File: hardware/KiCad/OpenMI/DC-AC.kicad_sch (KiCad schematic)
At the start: 31 parts, among them Q2 IPL60R125P7, Q3 IPL60R125P7, U1 IRS2304S

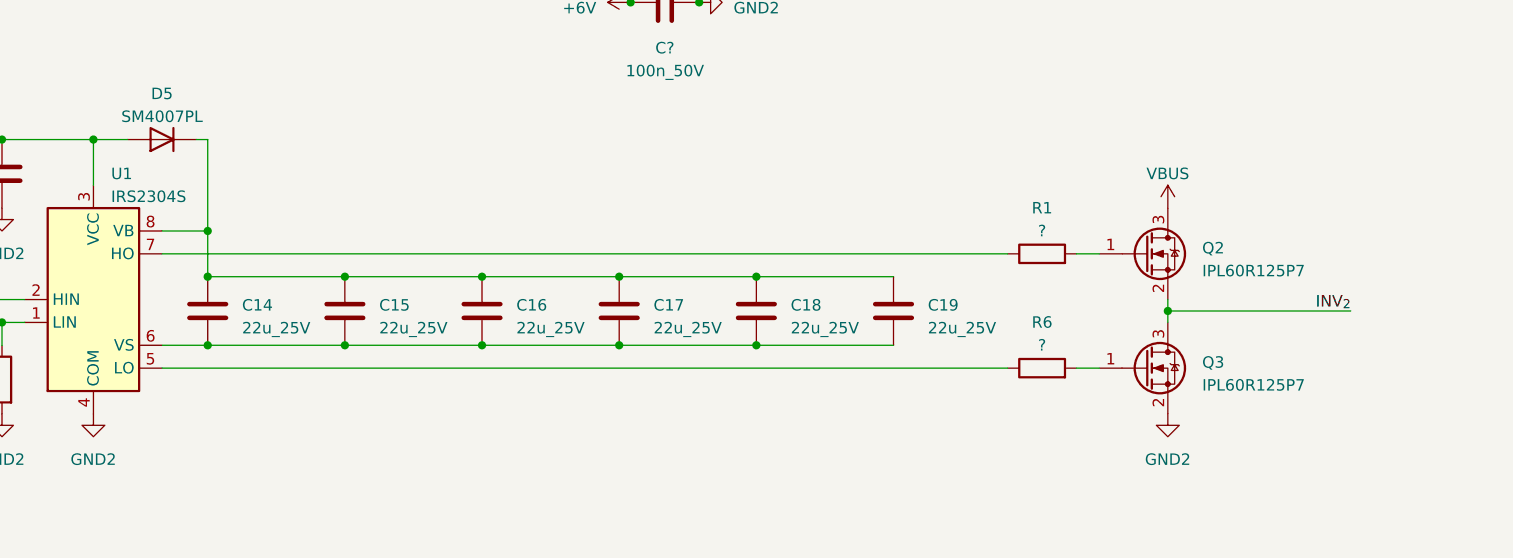
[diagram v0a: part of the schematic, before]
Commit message: fix(hw): connect high-side supply reference with half-bridge output
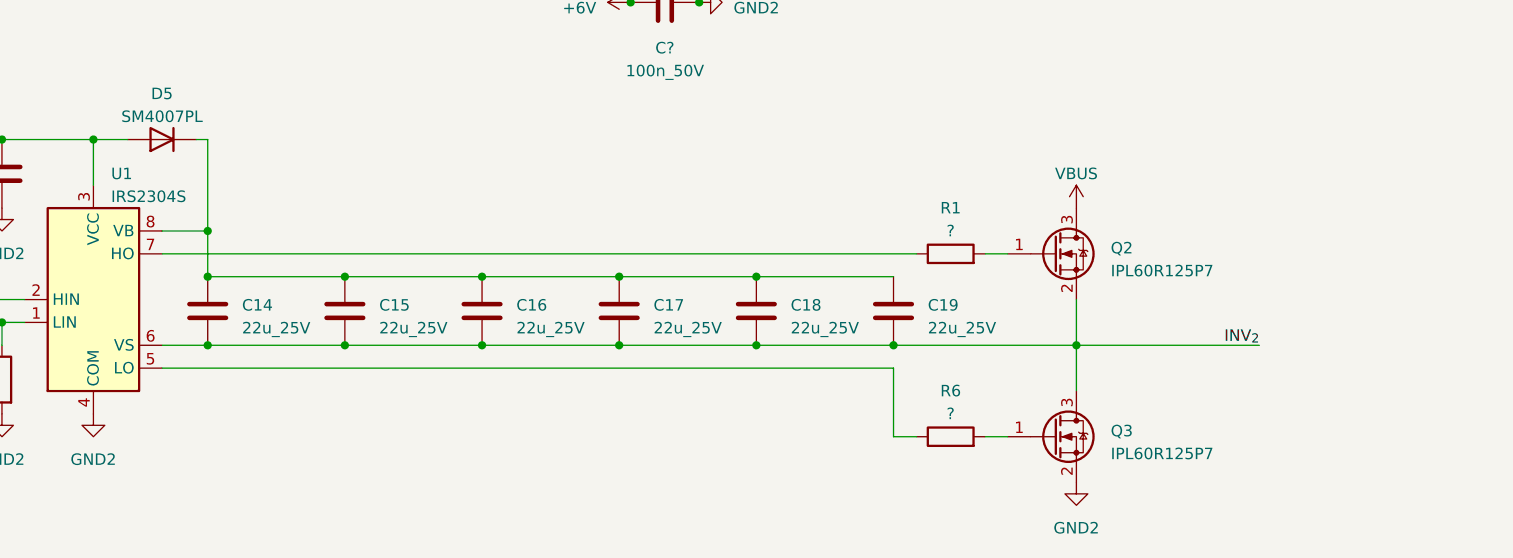
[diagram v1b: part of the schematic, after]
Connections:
- net INV_{2}: now also C14.2, C15.2, C16.2, C17.2, C18.2, C19.2, U1.6 (VS)
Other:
- moved on the sheet: Q2, Q3, R1, R6

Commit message: feat(hw): Remove unnecessary pull down restistors docs(hw): Add TODOS for power decoupling
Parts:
- removed R2, R3, R4, R5: 100K, Resistor_SMD:R_0603_1608Metric, symbol _R_0603:100K
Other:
- note added: "To do: - check dV/dt - enough capacity?"

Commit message: feat(hw): Add over temperature output
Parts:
- added C20: 1n_50V, Capacitor_SMD:C_0603_1608Metric, symbol _C_0603:1n_50V
- added R2: 100K, Resistor_SMD:R_0603_1608Metric, symbol _R_0603:100K
- added R3: 0R, Resistor_SMD:R_0603_1608Metric, symbol _R_0603:0R
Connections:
- net +6V: now also R2.1
- net GND: now also C20.2
- net at Q?.25 (~{SD}/OD): now also C20.1, R2.2, R3.2
- new net OverTemp: R3.1
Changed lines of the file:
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@@
   (junction (at 49.53 36.83) (diameter 0) (color 0 0 0 0)
+  )
+  (junction (at 88.9 102.87) (diameter 0) (color 0 0 0 0)
   )
   (junction (at 114.3 147.32) (diameter 0) (color 0 0 0 0)
@@
     (stroke (width 0) (type default))
   )
+  (wire (pts (xy 92.71 91.44) (xy 92.71 102.87))
+    (stroke (width 0) (type default))
+  )
   (wire (pts (xy 22.86 144.78) (xy 48.26 144.78))
     (stroke (width 0) (type default))
@@
     (stroke (width 0) (type default))
   )
+  (wire (pts (xy 107.95 91.44) (xy 92.71 91.44))
+    (stroke (width 0) (type default))
+  )
   (wire (pts (xy 29.21 124.46) (xy 45.72 124.46))
     (stroke (width 0) (type default))
@@
     (stroke (width 0) (type default))
   )
+  (wire (pts (xy 77.47 102.87) (xy 88.9 102.87))
+    (stroke (width 0) (type default))
+  )
   (wire (pts (xy 144.78 149.86) (xy 144.78 157.48))
     (stroke (width 0) (type default))
@@
     (stroke (width 0) (type default))
   )
+  (wire (pts (xy 88.9 102.87) (xy 92.71 102.87))
+    (stroke (width 0) (type default))
+  )
   (wire (pts (xy 105.41 68.58) (xy 113.03 68.58))
     (stroke (width 0) (type default))
@@
   )
   (wire (pts (xy 144.78 157.48) (xy 147.32 157.48))
+    (stroke (width 0) (type default))
+  )
+  (wire (pts (xy 62.23 102.87) (xy 69.85 102.87))
     (stroke (width 0) (type default))
   )
@@
     (effects (font (size 1.27 1.27)) (justify left bottom))
   )
+  (hierarchical_label "OverTemp" (shape output) (at 62.23 102.87 180) (fields_autoplaced)
+    (effects (font (size 1.27 1.27)) (justify right))
+  )
   (hierarchical_label "HIN_{F}" (shape input) (at 62.23 86.36 180) (fields_autoplaced)
     (effects (font (size 1.27 1.27)) (justify right))
@@
     )
   )
+  (symbol (lib_id "_R_0603:0R") (at 73.66 102.87 90) (unit 1)
+    (in_bom yes) (on_board yes) (dnp no) (fields_autoplaced)
+    (property "Reference" "R3" (at 73.66 97.79 90)
+      (effects (font (size 1.27 1.27)))
+    )
+    (property "Value" "0R" (at 73.66 100.33 90)
+      (effects (font (size 1.27 1.27)))
+    )
+    (property "Footprint" "Resistor_SMD:R_0603_1608Metric" (at 73.66 104.648 90)
+      (effects (font (size 1.27 1.27)) hide)
+    )
+    (property "Datasheet" "~" (at 73.66 102.87 0)
+      (effects (font (size 1.27 1.27)) hide)
+    )
+    (property "MF" "" (at 73.66 102.87 0)
+      (effects (font (size 1.27 1.27)) hide)
+    )
+    (property "MPN" "" (at 73.66 102.87 0)
+      (effects (font (size 1.27 1.27)) hide)
+    )
+    (property "OC_CONRAD" "" (at 73.66 102.87 0)
+      (effects (font (size 1.27 1.27)) hide)
+    )
+    (property "OC_FARNELL" "" (at 73.66 102.87 0)
+      (effects (font (size 1.27 1.27)) hide)
+    )
+    (property "OC_MOUSER" "603-AC0603FR-070RL" (at 73.66 102.87 0)
+      (effects (font (size 1.27 1.27)) hide)
+    )
+    (property "OC_REICHELT" "" (at 73.66 102.87 0)
+      (effects (font (size 1.27 1.27)) hide)
+    )
+    (pin "1")
+    (pin "2")
+    (instances
+      (project "OpenMI"
+        (path "/2d959e19-1572-42a0-a8fd-da8463ad4e66/19323a41-9b99-4de4-bfae-f2f828815be3"
+          (reference "R3") (unit 1)
+        )
+      )
+    )
+  )
   (symbol (lib_id "power:+6V") (at 88.9 67.31 0) (unit 1)
     (in_bom yes) (on_board yes) (dnp no) (fields_autoplaced)
@@
         (path "/2d959e19-1572-42a0-a8fd-da8463ad4e66/19323a41-9b99-4de4-bfae-f2f828815be3"
           (reference "C1") (unit 1)
+        )
+      )
+    )
+  )
+  (symbol (lib_id "_C_0603:1n_50V") (at 88.9 106.68 0) (mirror y) (unit 1)
+    (in_bom yes) (on_board yes) (dnp no)
+    (property "Reference" "C20" (at 85.09 106.045 0)
+      (effects (font (size 1.27 1.27)) (justify left))
+    )
+    (property "Value" "1n_50V" (at 85.09 108.585 0)
+      (effects (font (size 1.27 1.27)) (justify left))
+    )
+    (property "Footprint" "Capacitor_SMD:C_0603_1608Metric" (at 87.9348 110.49 0)
+      (effects (font (size 1.27 1.27)) hide)
+    )
+    (property "Datasheet" "~" (at 88.9 106.68 0)
+      (effects (font (size 1.27 1.27)) hide)
+    )
+    (property "MF" "" (at 88.9 106.68 0)
+      (effects (font (size 1.27 1.27)) hide)
+    )
+    (property "MPN" "" (at 88.9 106.68 0)
+      (effects (font (size 1.27 1.27)) hide)
+    )
+    (property "OC_CONRAD" "" (at 88.9 106.68 0)
+      (effects (font (size 1.27 1.27)) hide)
+    )
+    (property "OC_FARNELL" "" (at 88.9 106.68 0)
+      (effects (font (size 1.27 1.27)) hide)
+    )
+    (property "OC_MOUSER" "581-06035C102K" (at 88.9 106.68 0)
+      (effects (font (size 1.27 1.27)) hide)
+    )
+    (property "OC_REICHELT" "" (at 88.9 106.68 0)
+      (effects (font (size 1.27 1.27)) hide)
+    )
+    (pin "1")
+    (pin "2")
+    (instances
+      (project "OpenMI"
+        (path "/2d959e19-1572-42a0-a8fd-da8463ad4e66/19323a41-9b99-4de4-bfae-f2f828815be3"
+          (reference "C20") (unit 1)
         )
       )
@@
     )
   )
+  (symbol (lib_id "power:+6V") (at 88.9 95.25 0) (mirror y) (unit 1)
+    (in_bom yes) (on_board yes) (dnp no) (fields_autoplaced)
+    (property "Reference" "#PWR?" (at 88.9 99.06 0)
+      (effects (font (size 1.27 1.27)) hide)
+    )
+    (property "Value" "+6V" (at 88.9 91.44 0)
+      (effects (font (size 1.27 1.27)))
+    )
+    (property "Footprint" "" (at 88.9 95.25 0)
+      (effects (font (size 1.27 1.27)) hide)
+    )
+    (property "Datasheet" "" (at 88.9 95.25 0)
+      (effects (font (size 1.27 1.27)) hide)
+    )
+    (pin "1")
+    (instances
+      (project "OpenMI"
+        (path "/2d959e19-1572-42a0-a8fd-da8463ad4e66"
+          (reference "#PWR?") (unit 1)
+        )
+        (path "/2d959e19-1572-42a0-a8fd-da8463ad4e66/19323a41-9b99-4de4-bfae-f2f828815be3"
+          (reference "#PWR016") (unit 1)
+        )
+      )
+    )
+  )
   (symbol (lib_id "Device:D") (at 135.89 83.82 270) (unit 1)
     (in_bom yes) (on_board yes) (dnp no) (fields_autoplaced)
@@
         (path "/2d959e19-1572-42a0-a8fd-da8463ad4e66/19323a41-9b99-4de4-bfae-f2f828815be3"
           (reference "R6") (unit 1)
+        )
+      )
+    )
+  )
+  (symbol (lib_id "power:GND2") (at 88.9 110.49 0) (unit 1)
+    (in_bom yes) (on_board yes) (dnp no) (fields_autoplaced)
+    (property "Reference" "#PWR?" (at 88.9 116.84 0)
+      (effects (font (size 1.27 1.27)) hide)
+    )
+    (property "Value" "GND2" (at 88.9 115.57 0)
+      (effects (font (size 1.27 1.27)))
+    )
+    (property "Footprint" "" (at 88.9 110.49 0)
+      (effects (font (size 1.27 1.27)) hide)
+    )
+    (property "Datasheet" "" (at 88.9 110.49 0)
+      (effects (font (size 1.27 1.27)) hide)
+    )
+    (pin "1")
+    (instances
+      (project "OpenMI"
+        (path "/2d959e19-1572-42a0-a8fd-da8463ad4e66"
+          (reference "#PWR?") (unit 1)
+        )
+        (path "/2d959e19-1572-42a0-a8fd-da8463ad4e66/19323a41-9b99-4de4-bfae-f2f828815be3"
+          (reference "#PWR017") (unit 1)
         )
       )
@@
         )
       )
+    )
+  )
+  (symbol (lib_id "_R_0603:100K") (at 88.9 99.06 0) (mirror y) (unit 1)
+    (in_bom yes) (on_board yes) (dnp no)
+    (property "Reference" "R2" (at 86.36 98.425 0)
+      (effects (font (size 1.27 1.27)) (justify left))
+    )
+    (property "Value" "100K" (at 86.36 100.965 0)
+      (effects (font (size 1.27 1.27)) (justify left))
+    )
+    (property "Footprint" "Resistor_SMD:R_0603_1608Metric" (at 90.678 99.06 90)
+      (effects (font (size 1.27 1.27)) hide)
+    )
+    (property "Datasheet" "~" (at 88.9 99.06 0)
+      (effects (font (size 1.27 1.27)) hide)
+    )
+    (property "MF" "" (at 88.9 99.06 0)
+      (effects (font (size 1.27 1.27)) hide)
+    )
+    (property "MPN" "" (at 88.9 99.06 0)
+      (effects (font (size 1.27 1.27)) hide)
+    )
+    (property "OC_CONRAD" "" (at 88.9 99.06 0)
+      (effects (font (size 1.27 1.27)) hide)
+    )
+    (property "OC_FARNELL" "" (at 88.9 99.06 0)
+      (effects (font (size 1.27 1.27)) hide)
+    )
+    (property "OC_MOUSER" "603-AC0603FR-07100KL" (at 88.9 99.06 0)
+      (effects (font (size 1.27 1.27)) hide)
+    )
+    (property "OC_REICHELT" "" (at 88.9 99.06 0)
+      (effects (font (size 1.27 1.27)) hide)
+    )
+    (pin "1")
+    (pin "2")
+    (instances
+      (project "OpenMI"
+        (path "/2d959e19-1572-42a0-a8fd-da8463ad4e66/19323a41-9b99-4de4-bfae-f2f828815be3"
+          (reference "R2") (unit 1)
+        )
+      )

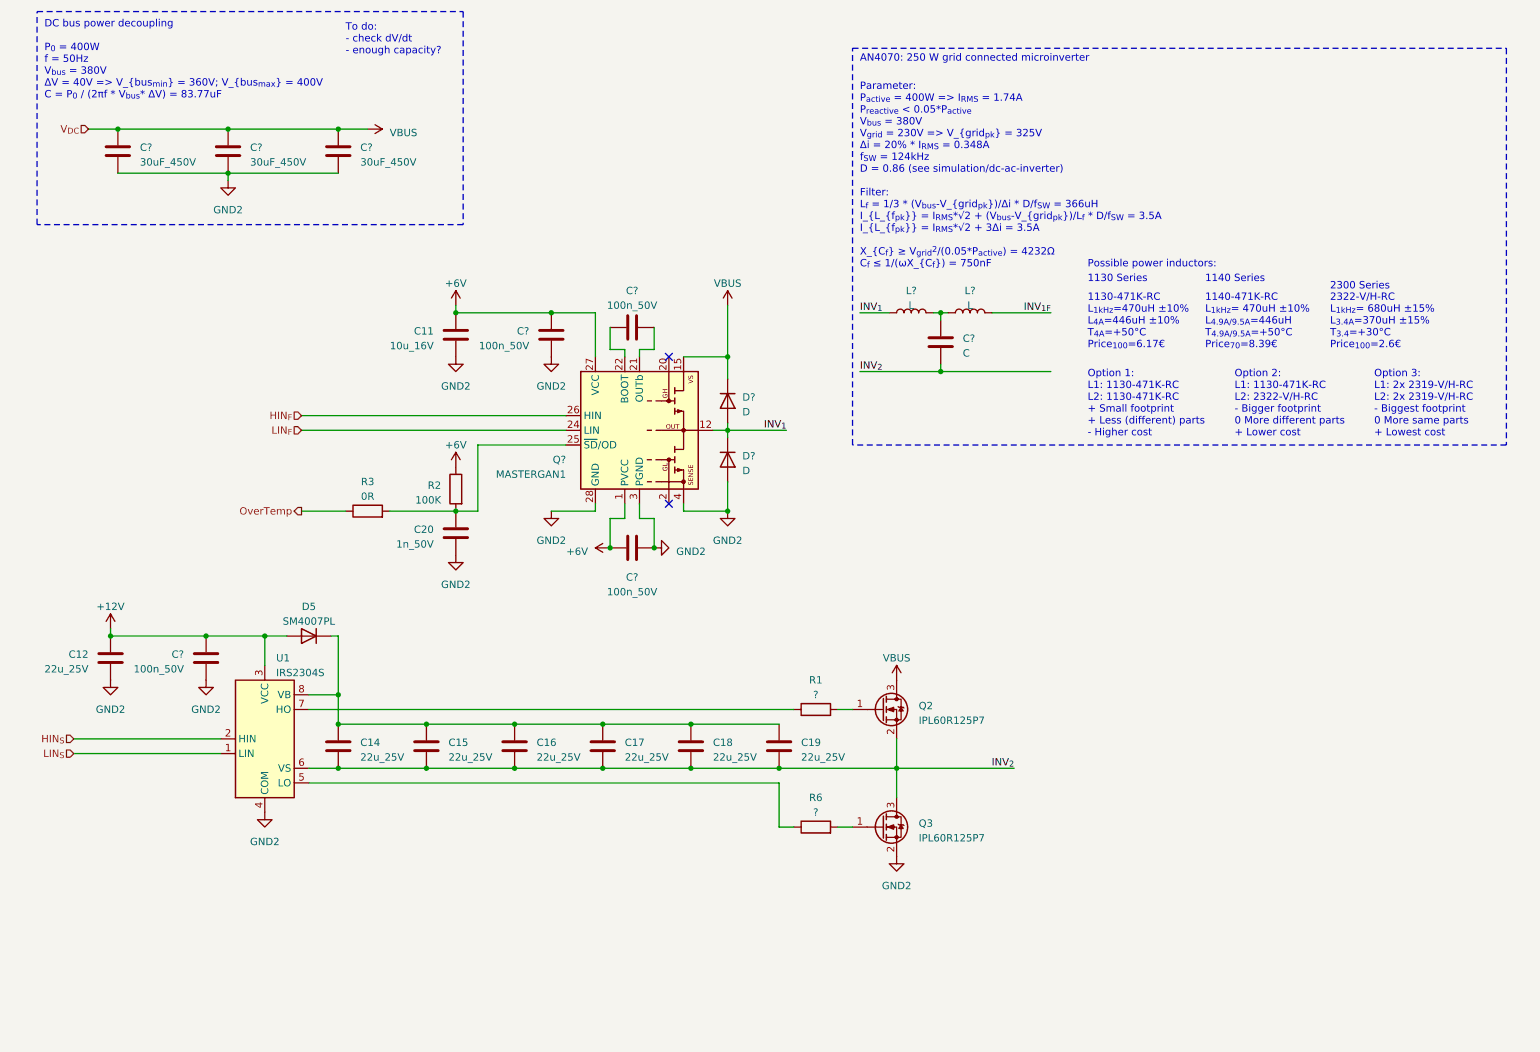
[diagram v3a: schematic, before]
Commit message: docs(hw): Add references for formulas
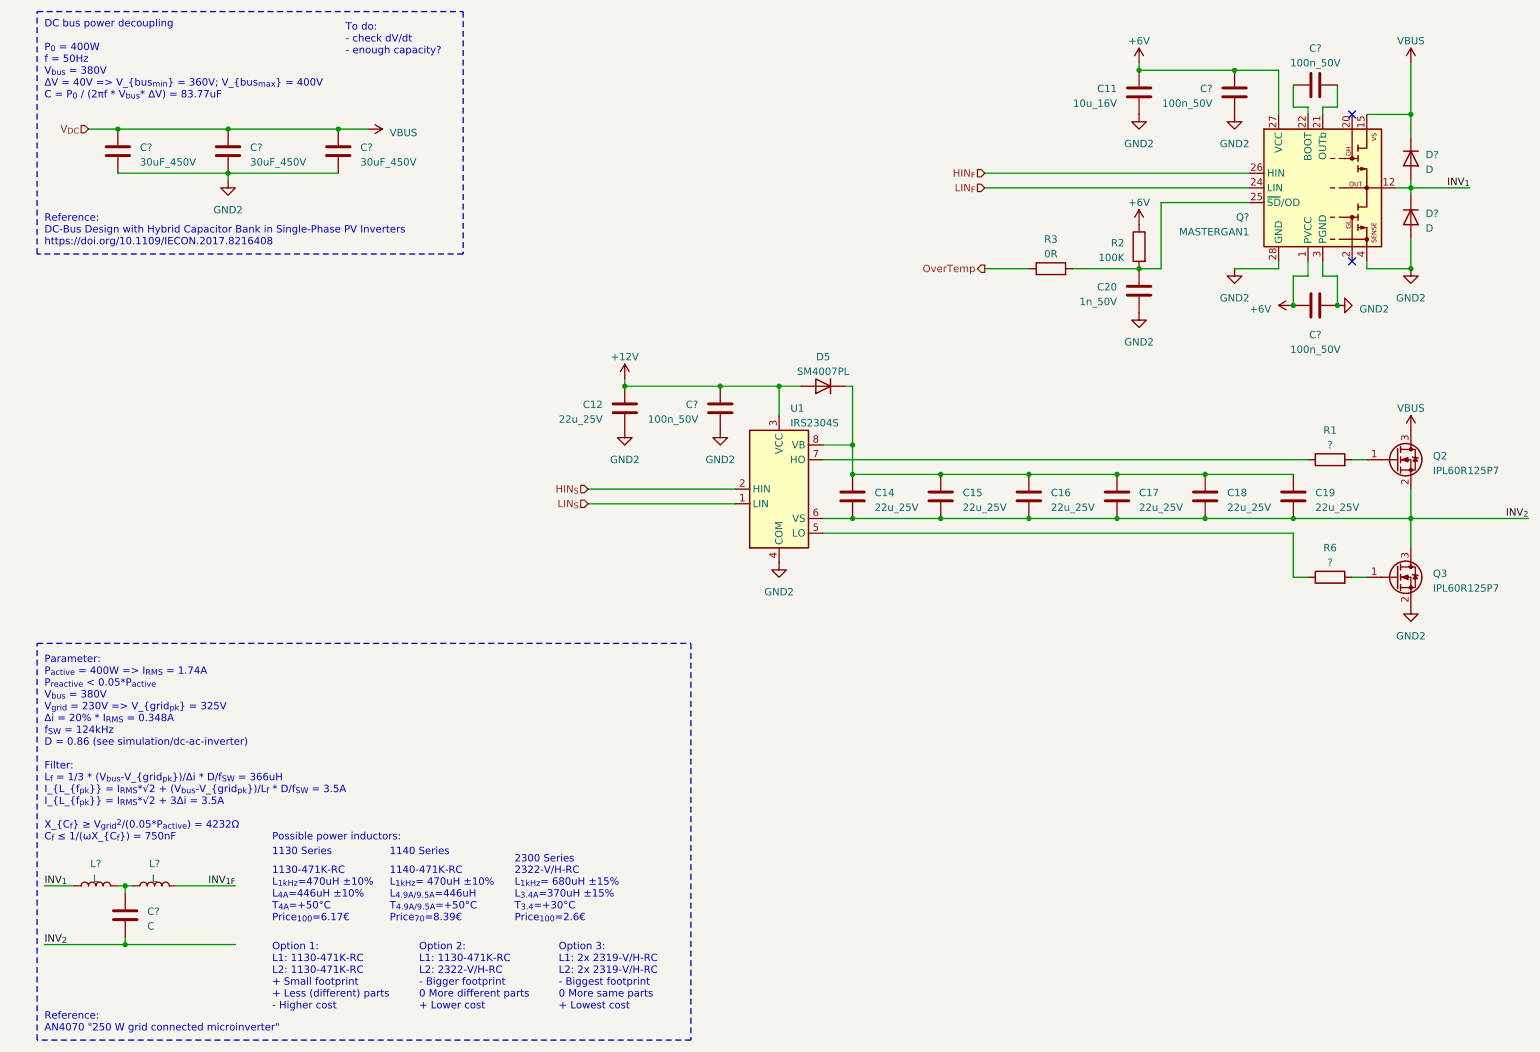
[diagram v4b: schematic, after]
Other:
- note added: "Reference: AN4070 "250 W grid connected microinverter""
- note added: "Reference: DC-Bus Design with Hybrid Capacitor Bank in Single-Phase PV Inverters https://doi.org/10.1109/IECON.2017.8216408"
- note removed: "AN4070: 250 W grid connected microinverter"
- moved on the sheet: C11, C12, C14, C15, C16, C17, C18, C19, C20, C?, D5, D?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
